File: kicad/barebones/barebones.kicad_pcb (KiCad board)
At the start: 2 copper layers, 55 x 67 mm, 12 parts, among them J101 PAL-1 Expansion Connector, J102 G27, J103 WE, SW101 PICO RESET, SW102 SW_DIP_x08, U101 74LS01, U102 74LS145, U104 Pico

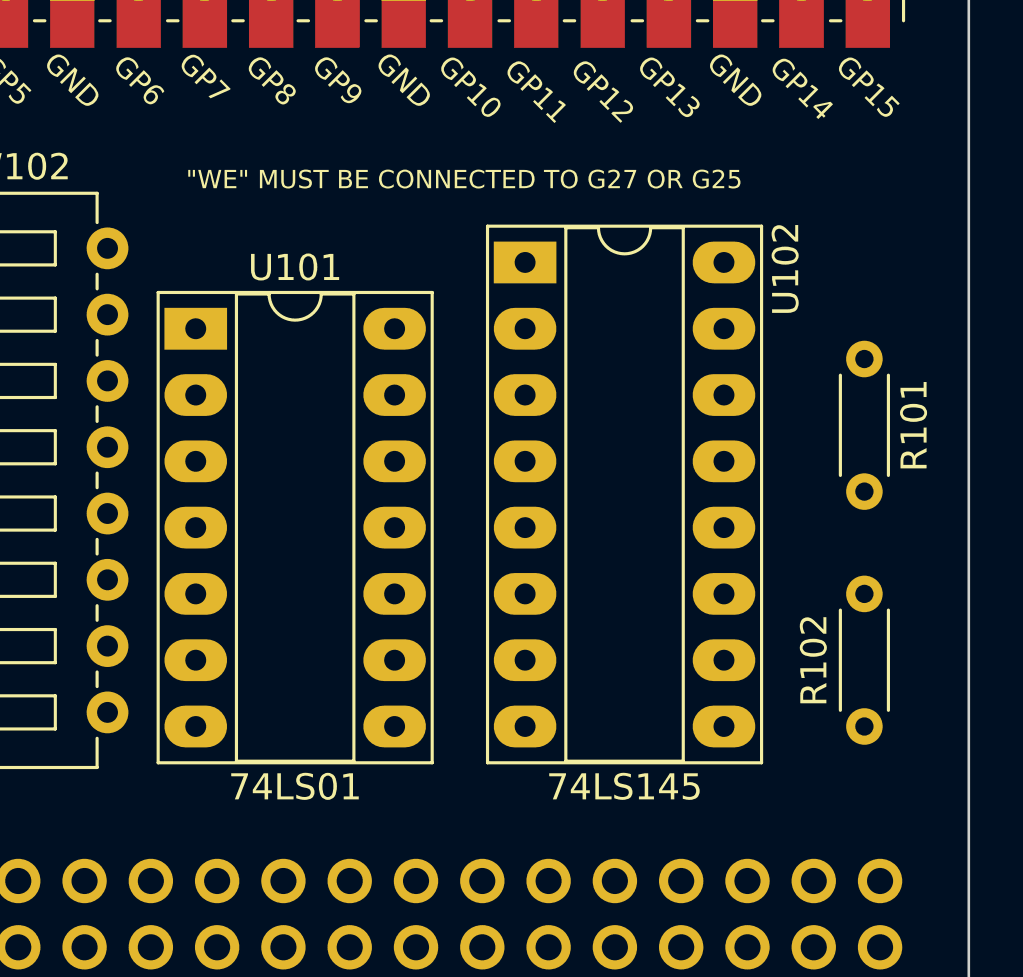
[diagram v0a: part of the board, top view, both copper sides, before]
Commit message: Updated code so that CS works correctly, started next PCB version
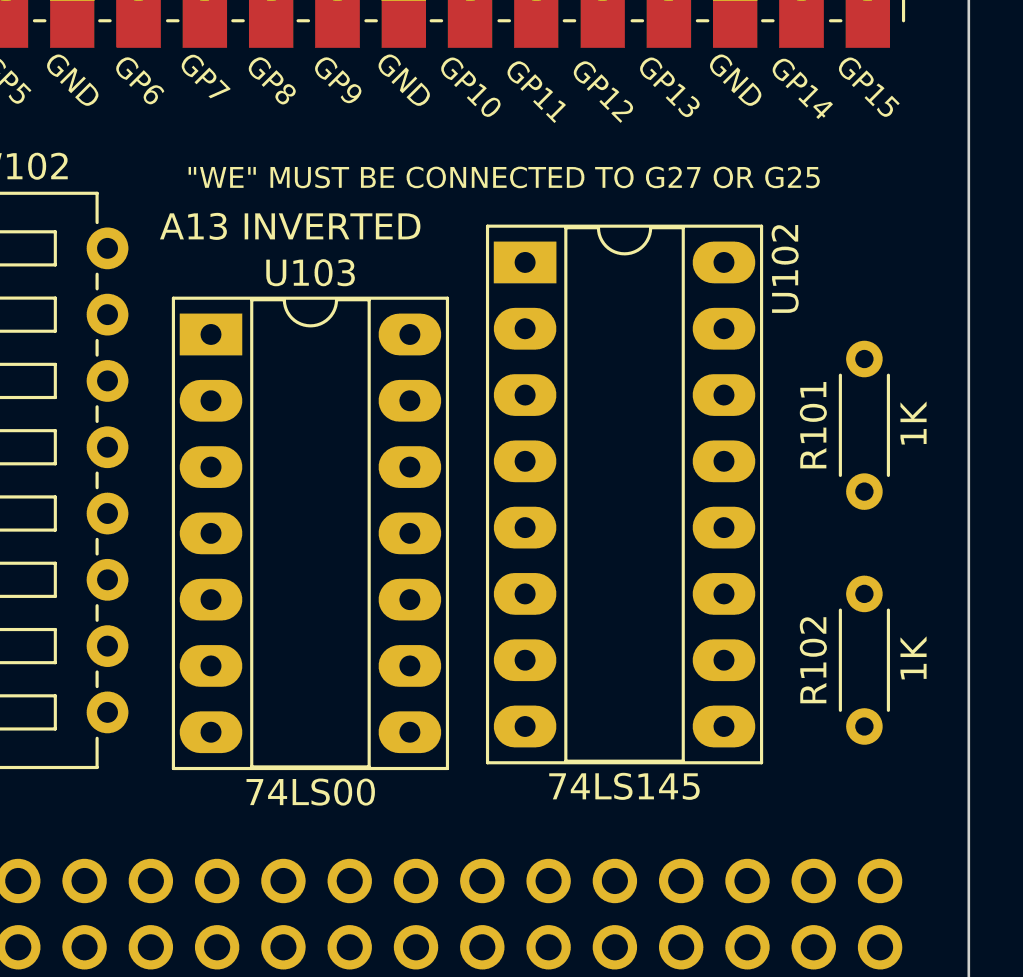
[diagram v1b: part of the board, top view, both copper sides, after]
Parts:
- removed U101: 74LS01, Package_DIP:DIP-14_W7.62mm_Socket_LongPads
- added U103: 74LS00, Package_DIP:DIP-14_W7.62mm_Socket_LongPads, F.Cu at (146.0, 90.5)
- R101, R102: value 100K -> 1K
- moved R101 5.08 mm to (171.0, 96.5), turned to 90 degrees

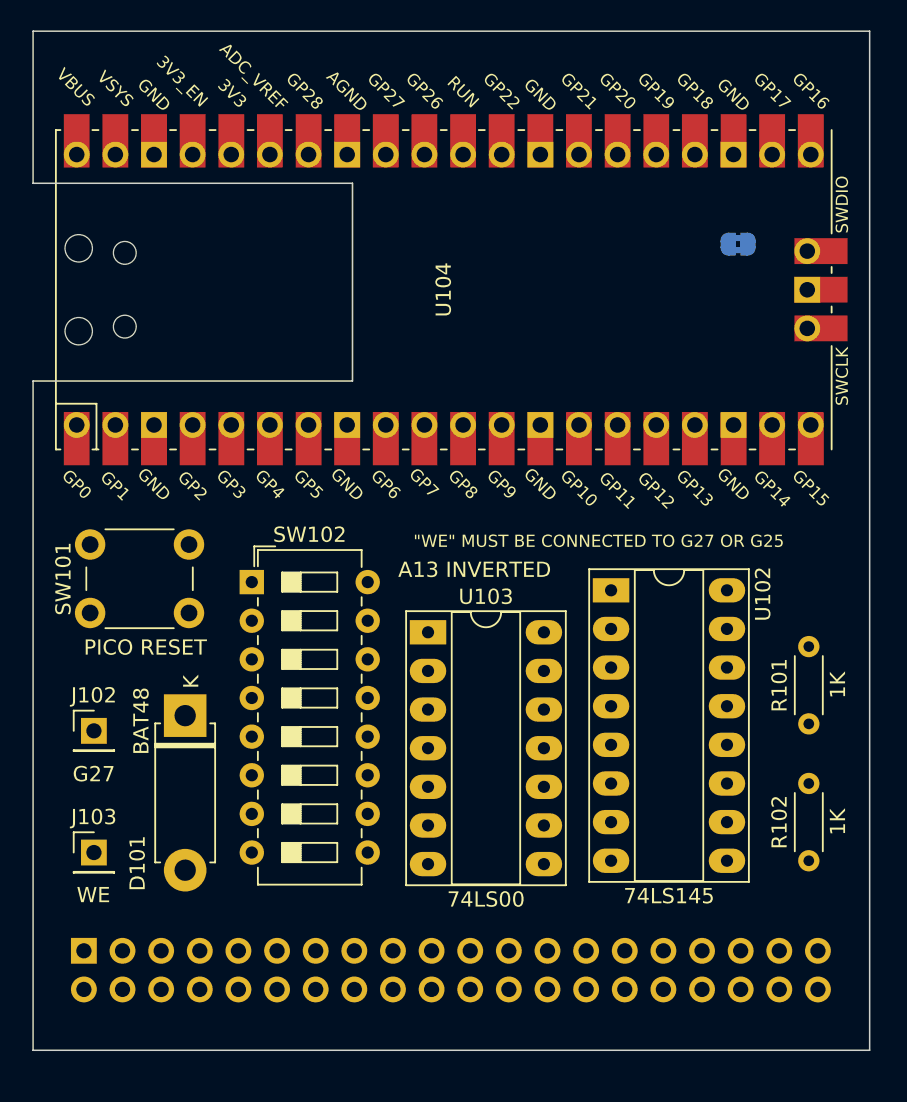
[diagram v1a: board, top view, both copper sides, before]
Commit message: RAM working and updating. PHI2 respected.
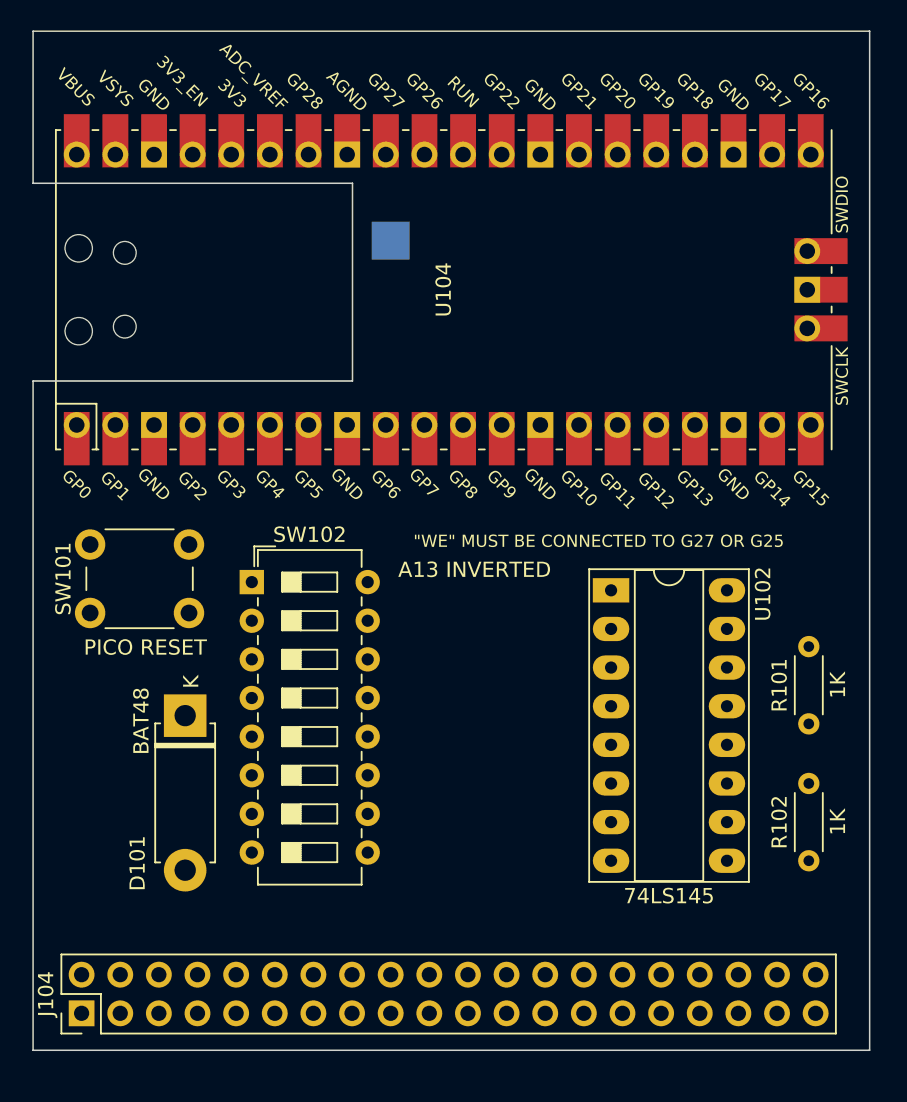
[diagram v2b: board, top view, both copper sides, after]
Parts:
- removed J101: PAL-1 Expansion Connector, Connector_PinHeader_2.54mm:PinHeader_2x20_P2.54mm_Horizontal
- removed J102: G27, Connector_PinHeader_2.54mm:PinHeader_1x01_P2.54mm_Vertical
- removed J103: WE, Connector_PinHeader_2.54mm:PinHeader_1x01_P2.54mm_Vertical
- removed JP101: SolderJumper_2_Bridged, Jumper:SolderJumper-2_P1.3mm_Bridged2Bar_RoundedPad1.0x1.5mm
- removed U103: 74LS00, Package_DIP:DIP-14_W7.62mm_Socket_LongPads
- added J104: PAL-1 Expansion Connector, Connector_PinHeader_2.54mm:PinHeader_2x20_P2.54mm_Vertical, F.Cu at (123.2, 115.6)
- added TP101: PIN25/TP5 CONNECT, TestPoint:TestPoint_Pad_2.5x2.5mm, B.Cu at (143.5, 64.8)
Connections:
- U104 pad 17: Net-(U104-GPIO13) -> A13
- U104 pad 32: Net-(J102-Pin_1) -> RW
- U104 pad 38: Net-(JP101-A) -> unconnected-(U104-GND-Pad38)

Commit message: Bit of PCB cleanup for removed features.
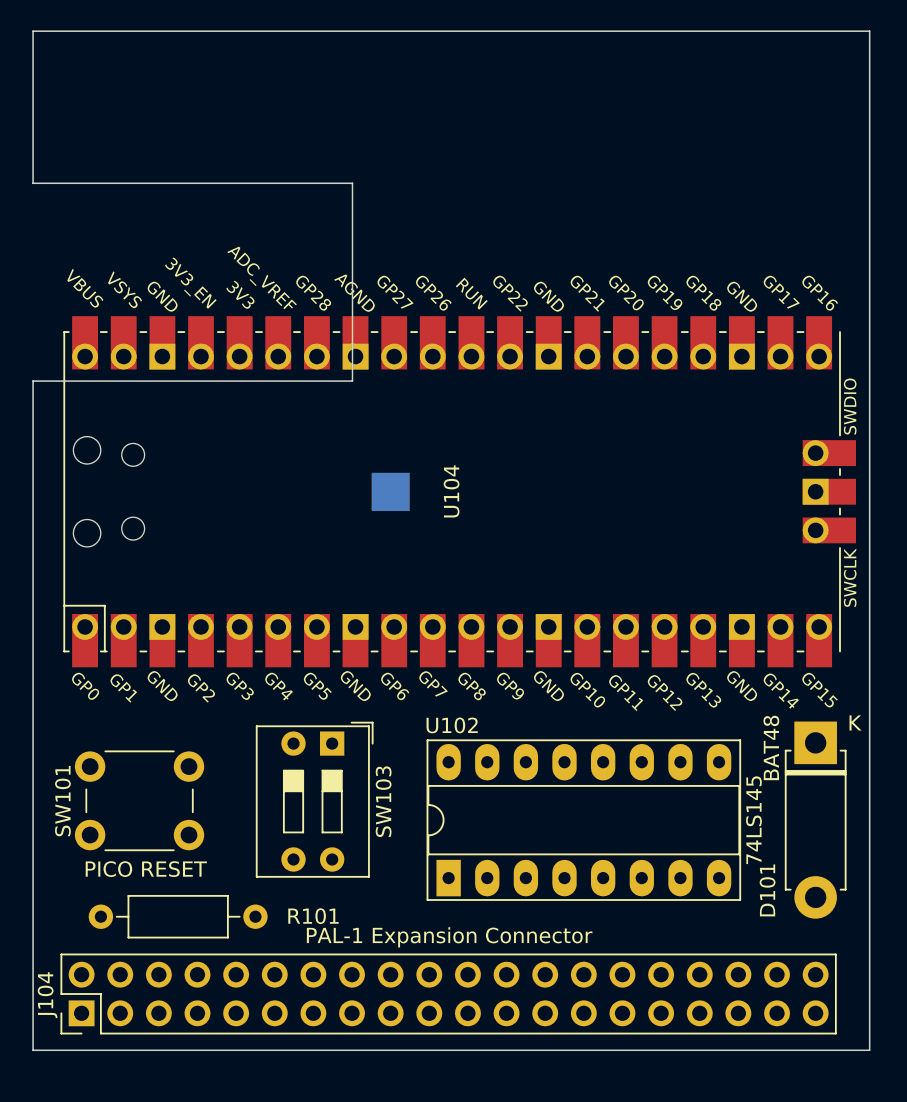
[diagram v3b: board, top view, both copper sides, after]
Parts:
- removed R102: 1K, Resistor_THT:R_Axial_DIN0204_L3.6mm_D1.6mm_P5.08mm_Horizontal
- removed SW102: SW_DIP_x08, Button_Switch_THT:SW_DIP_SPSTx08_Slide_6.7x21.88mm_W7.62mm_P2.54mm_LowProfile
- added SW103: SW_DIP_x02, Button_Switch_THT:SW_DIP_SPSTx02_Slide_9.78x7.26mm_W7.62mm_P2.54mm, F.Cu at (139.7, 97.8)
- R101: footprint Resistor_THT:R_Axial_DIN0204_L3.6mm_D1.6mm_P5.08mm_Horizontal -> Resistor_THT:R_Axial_DIN0207_L6.3mm_D2.5mm_P10.16mm_Horizontal
- TP101: value PIN25/TP5 CONNECT -> TestPoint
- moved R101 48.2 mm to (124.5, 109.2), turned to 0 degrees
- moved D101 41.5 mm to (171.4, 97.8)
- moved U102 21.7 mm to (147.3, 106.7), turned to 90 degrees
- moved TP101 16.5 mm to (143.5, 81.3)
- moved SW101 14.6 mm to (123.8, 99.3)
- moved U104 13.3 mm to (147.6, 81.3)
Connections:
- U102 pad 2: Net-(U102-Q1) -> unconnected-(U102-Q1-Pad2)
- U102 pad 3: Net-(U102-Q2) -> unconnected-(U102-Q2-Pad3)
- U102 pad 4: Net-(U102-Q3) -> unconnected-(U102-Q3-Pad4)
- U102 pad 5: Net-(U102-Q4) -> unconnected-(U102-Q4-Pad5)
- U102 pad 6: Net-(U102-Q5) -> unconnected-(U102-Q5-Pad6)
- U102 pad 7: Net-(U102-Q6) -> unconnected-(U102-Q6-Pad7)
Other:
- board text added: "Connect to TP5 on the Pico"
- board text removed: "A13 INVERTED"
- board text removed: "{dblquote}WE{dblquote} MUST BE CONNECTED TO G27 OR G25"

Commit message: New PCB that is 100% software defined
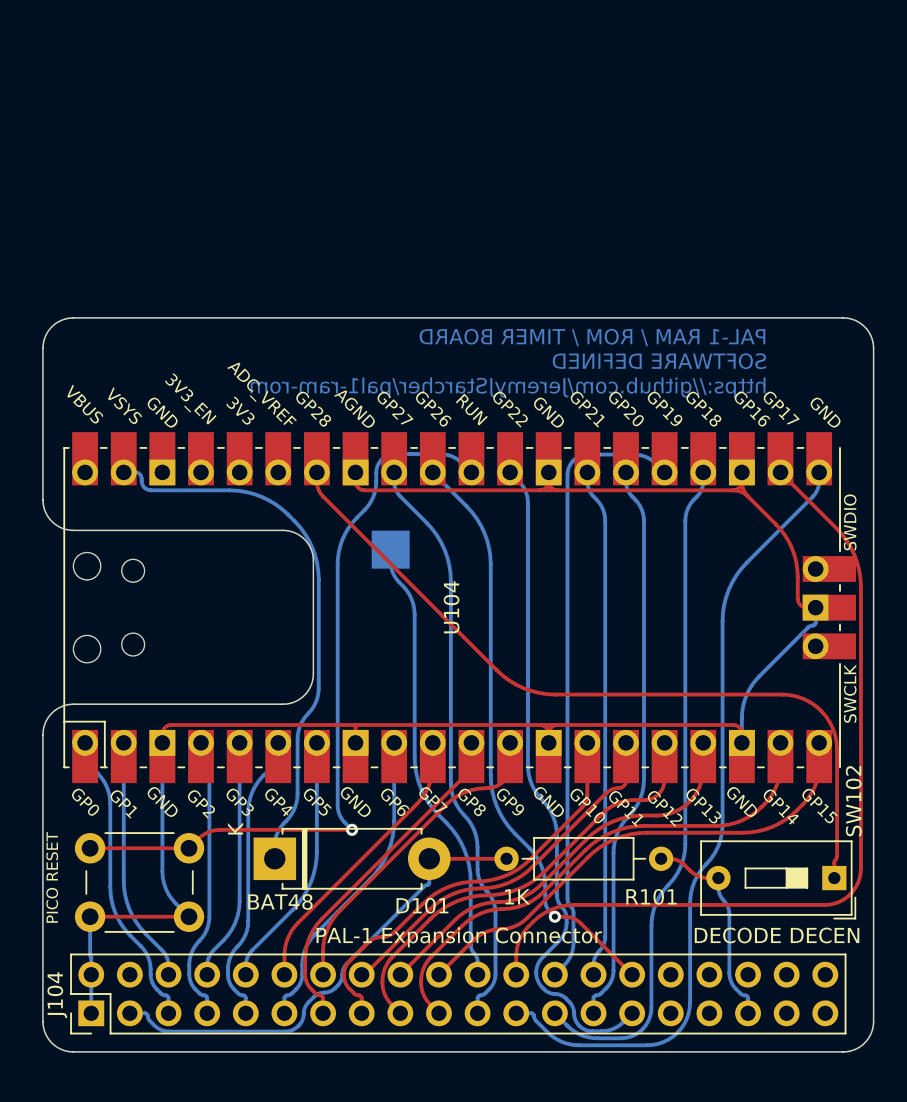
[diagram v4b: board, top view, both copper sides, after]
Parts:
- removed SW103: SW_DIP_x02, Button_Switch_THT:SW_DIP_SPSTx02_Slide_9.78x7.26mm_W7.62mm_P2.54mm
- removed U102: 74LS145, Package_DIP:DIP-16_W7.62mm_Socket_LongPads
- added SW102: SW_DIP_x01, Button_Switch_THT:SW_DIP_SPSTx01_Slide_9.78x4.72mm_W7.62mm_P2.54mm, F.Cu at (172.7, 106.7)
- TP101: value TestPoint -> CONNECT TO TP5 ON PICO
- moved D101 36.4 mm to (135.9, 105.4), turned to 0 degrees
- moved R101 26.9 mm to (151.1, 105.4)
- moved U104 7.62 mm to (147.6, 88.9)
- moved SW101 5.37 mm to (123.8, 104.7)
- moved TP101 3.81 mm to (143.5, 85.1)
- moved J104 0.64 mm to (123.8, 115.6)
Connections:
- U104 pad 34: CS -> Net-(U104-GPIO28_ADC2)
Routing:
- net GND: track 0.00 -> 120.3 mm
- net D1: track 0.00 -> 54.9 mm
- net D0: track 0.00 -> 51.5 mm
- net Net-(U104-GPIO28_ADC2): track 0.00 -> 51.1 mm
- net Net-(SW101-A): track 0.00 -> 49.5 mm, vias 0 -> 1
- net D2: track 0.00 -> 44.1 mm
- net D6: track 0.00 -> 43.4 mm
- net D3: track 0.00 -> 40.9 mm
- net D7: track 0.00 -> 38.4 mm, vias 0 -> 1
- net RW: track 0.00 -> 38.0 mm
- net D4: track 0.00 -> 37.0 mm
- net Net-(D101-K): track 0.00 -> 35.9 mm
- net A14: track 0.00 -> 33.8 mm
- net D5: track 0.00 -> 33.5 mm
- net A15: track 0.00 -> 32.1 mm
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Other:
- board size 55 x 67 mm -> 54.6 x 48.3 mm
- board text added: "CONNECT TP101 TO TP5 ON PICO."
- board text added: "ONLY ONE BOARD ON tHE BUS CAN DECODE DECEN TO ENABLE THE PAL-1s ADDRESS INTERNAL ADDRESSING"
- board text added: "PAL-1 RAM / ROM / TIMER BOARD SOFTWARE DEFINED https://github.com/JeremyJStarcher/pal1-ram-rom"
- board text removed: "Connect to TP5 on the Pico"

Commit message: Fixed up PCB design due to flat in last PCB
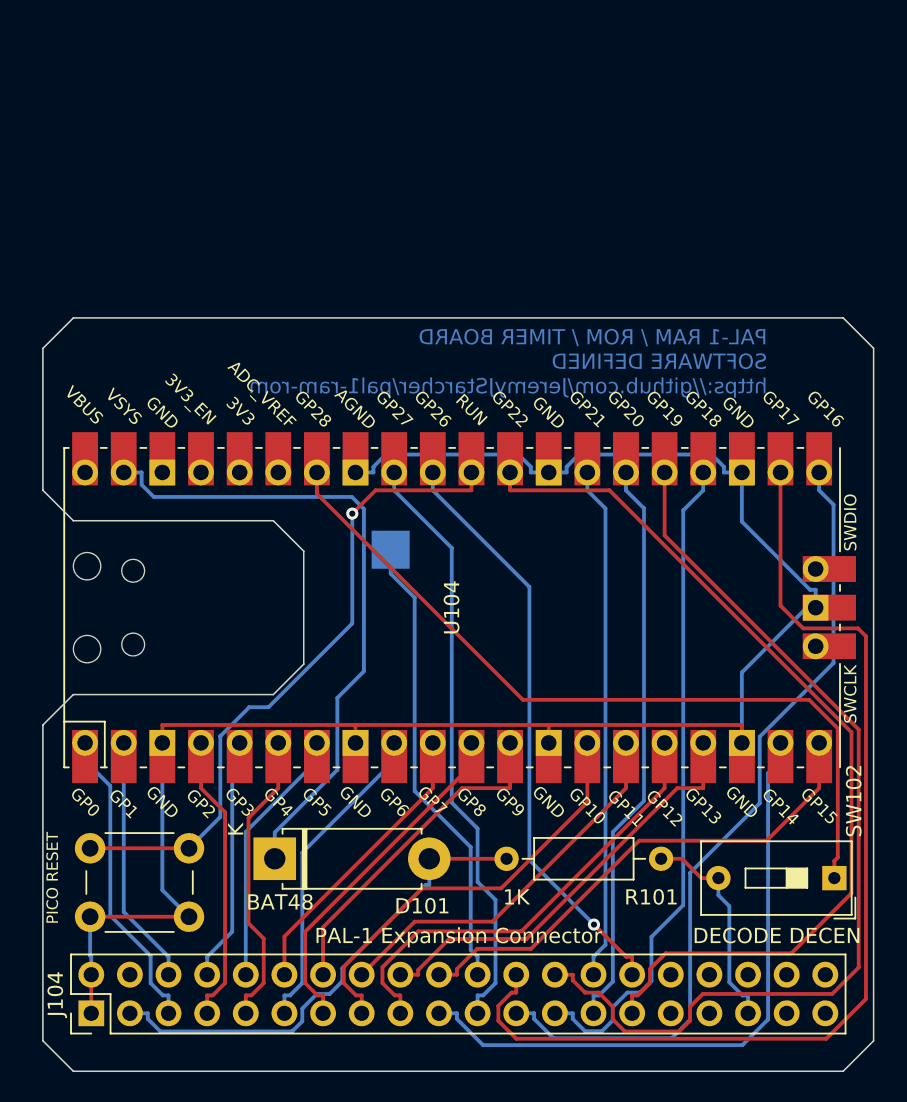
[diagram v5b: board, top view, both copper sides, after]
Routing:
- net D3: track 40.9 -> 62.3 mm
- net D6: track 43.4 -> 59.7 mm
- net D1: track 54.9 -> 68.5 mm
- net A14: track 33.8 -> 41.9 mm
- net Net-(D101-K): track 35.9 -> 42.7 mm
- net Net-(SW101-A): track 49.5 -> 43.3 mm
- net GND: track 120.3 -> 118.7 mm
- net D0: track 51.5 -> 53.1 mm
- net A12: track 29.0 -> 30.1 mm
- net A15: track 32.1 -> 33.3 mm
- net A13: track 27.0 -> 28.2 mm
- net A9: track 21.1 -> 22.2 mm
- net RW: track 38.0 -> 39.0 mm
- net A10: track 27.3 -> 28.2 mm
- net Net-(U104-GPIO28_ADC2): track 51.1 -> 52.0 mm
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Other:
- board size 54.6 x 48.3 mm -> 54.6 x 49.5 mm
- board text added: "ONLY ONE BOARD ON THE BUS CAN DECODE DECEN TO ENABLE THE PAL-1s ADDRESS INTERNAL ADDRESSING"
- board text removed: "ONLY ONE BOARD ON tHE BUS CAN DECODE DECEN TO ENABLE THE PAL-1s ADDRESS INTERNAL ADDRESSING"
